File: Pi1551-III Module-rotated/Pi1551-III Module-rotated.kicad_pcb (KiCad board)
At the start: 2 copper layers, 100 x 100 mm, 35 parts, among them J1 DC IN, J3 TCBM, J4 Mini-DIN-7, J8 Module_Panel, M1 Mounting, M2 Mounting, M3 Mounting, M4 Mounting, Q1 MMBT3904, Q2 MMBT3904, Q3 MMBT3904, Q4 MMBT3904

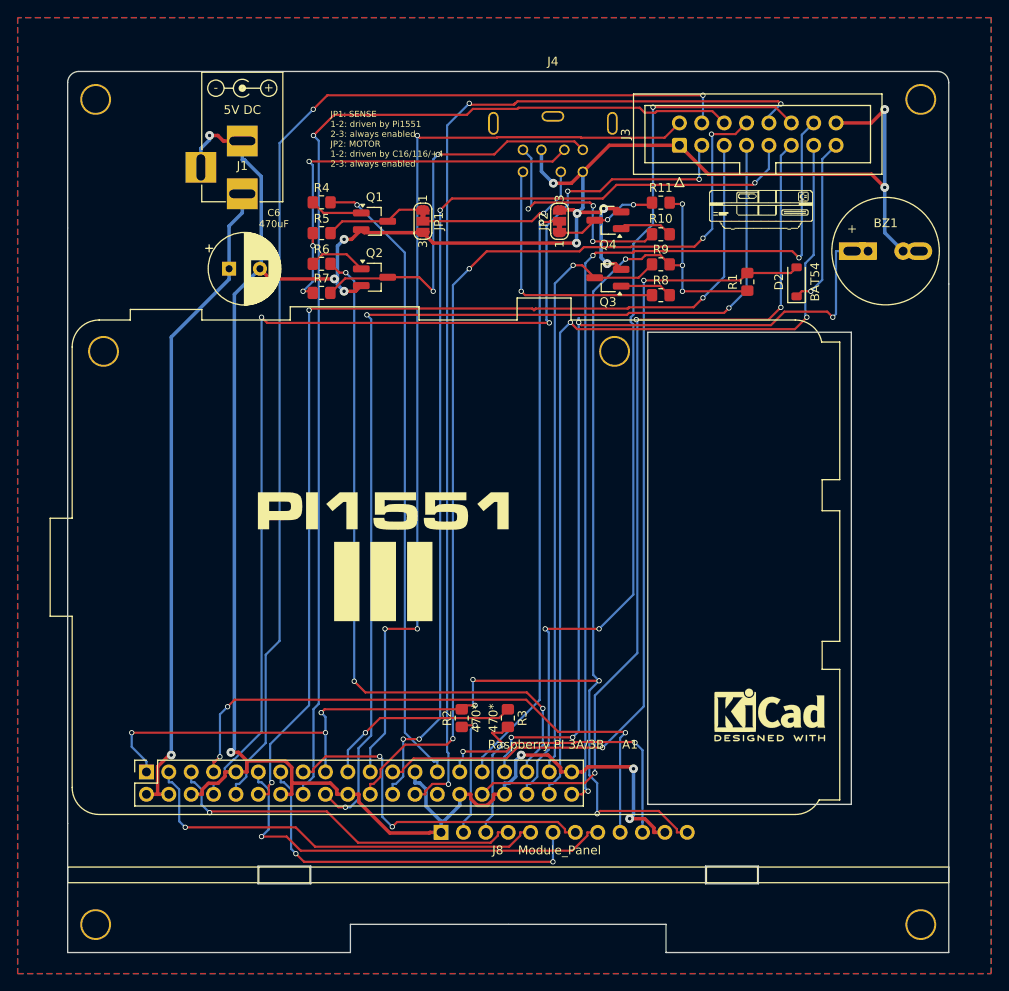
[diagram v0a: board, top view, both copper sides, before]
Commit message: all 10K resistors to 3.3K, JLPCB part numbers for 470R resistors, 1.2mm track width for 5V - as short as possible
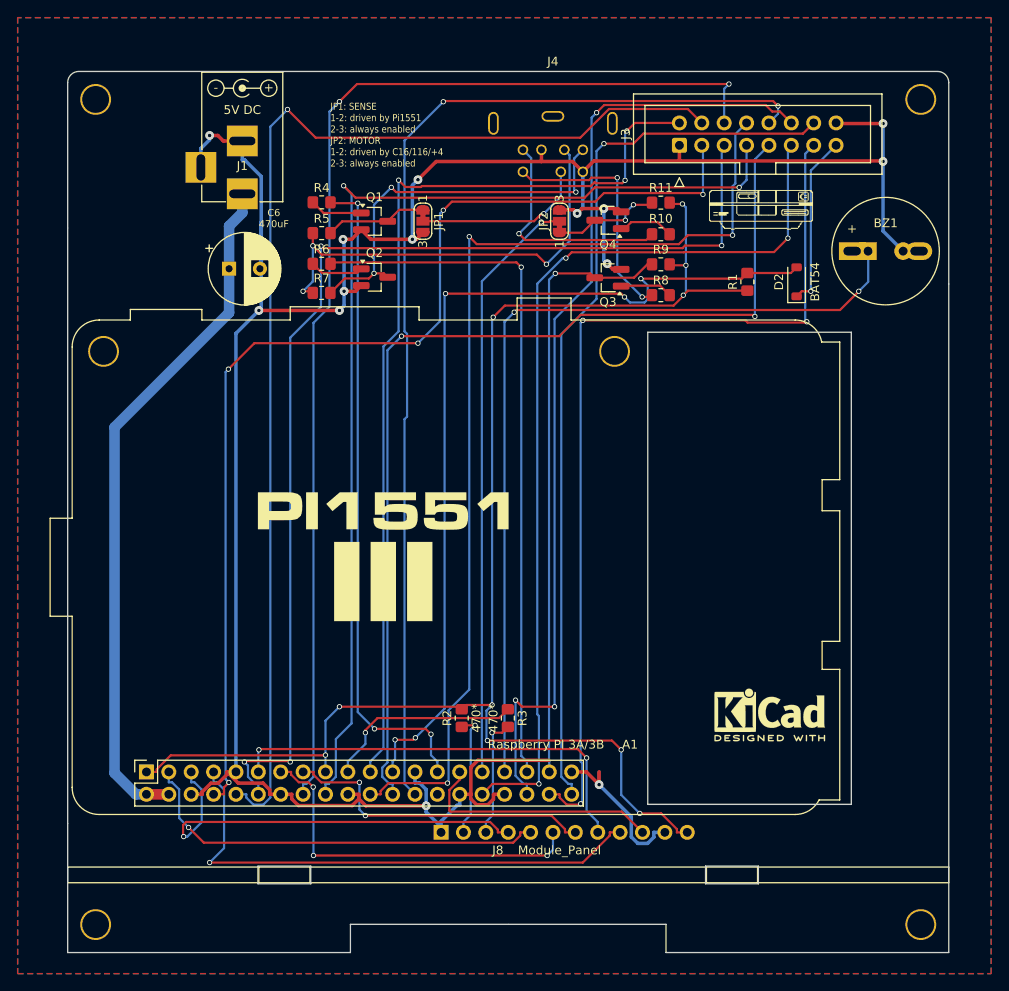
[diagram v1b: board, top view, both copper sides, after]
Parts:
- R1, R10, R11, R4, R5, R6, R7, R8, R9: value 10k -> 3.3K
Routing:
- net SW4_BACK: track 66.7 -> 59.9 mm, vias 3 -> 1
- net I2C_SCL: track 41.8 -> 48.2 mm
- net /DIO4: track 124.8 -> 130.2 mm, vias 1 -> 2
- net SW5_INSERT: track 33.0 -> 27.8 mm, vias 2 -> 0
- net /DIO3: track 122.4 -> 127.0 mm, vias 3 -> 4
- net /DIO6: track 112.0 -> 116.6 mm, vias 4 -> 3
- net /DIO2: track 129.7 -> 134.2 mm, vias 2 -> 1
- net /~{RESET_3V3}: track 98.1 -> 102.4 mm, vias 2 -> 5
- net /STATUS0: track 104.7 -> 108.9 mm
- net +5V: track 74.8 -> 78.9 mm, vias 1 -> 0
- net SW2_UP: track 39.9 -> 35.9 mm
- net /TAP_SENSE: track 71.5 -> 74.8 mm, vias 1 -> 3
- net /DIO7: track 111.7 -> 114.9 mm, vias 4 -> 2
- net /ACK: track 102.5 -> 105.5 mm, vias 2 -> 3
- net +3.3V: track 172.4 -> 169.8 mm, vias 11 -> 10
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
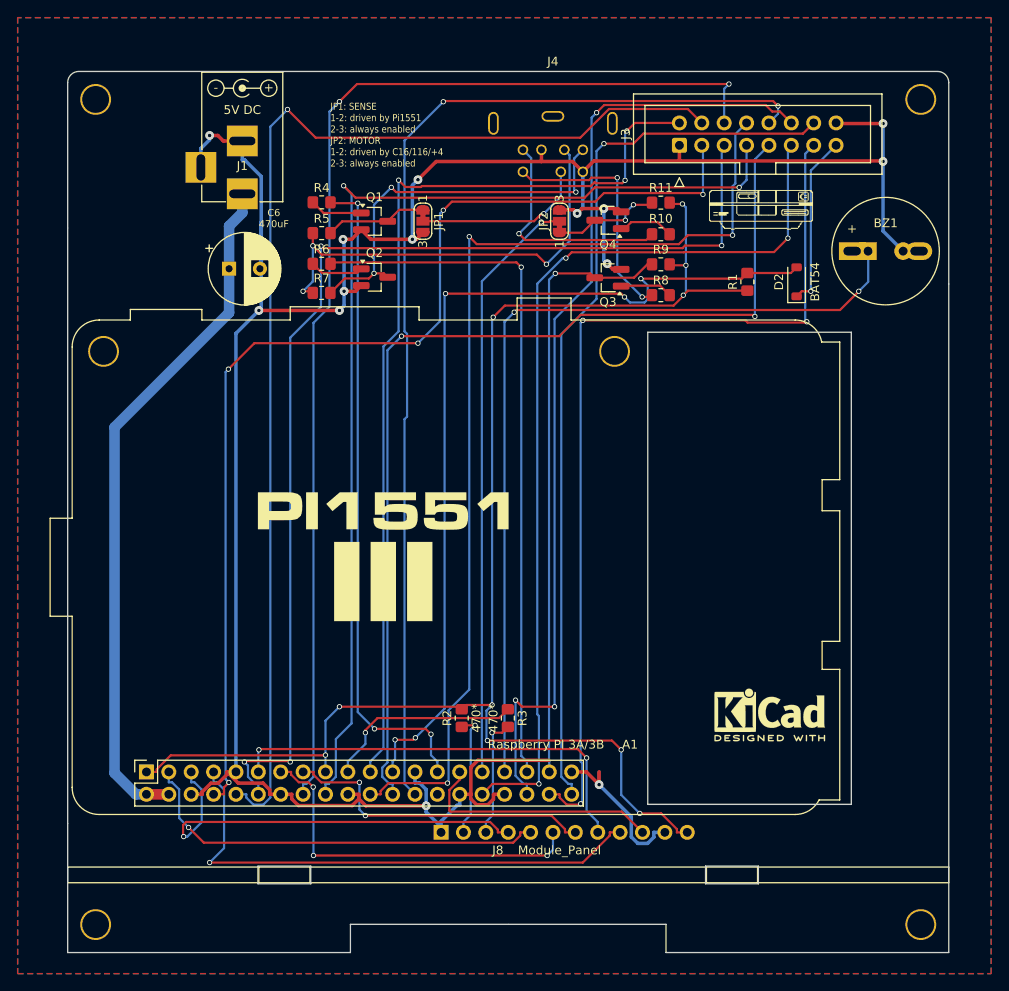
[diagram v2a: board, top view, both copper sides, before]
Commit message: revision 2 - pullups on all TCBM lines
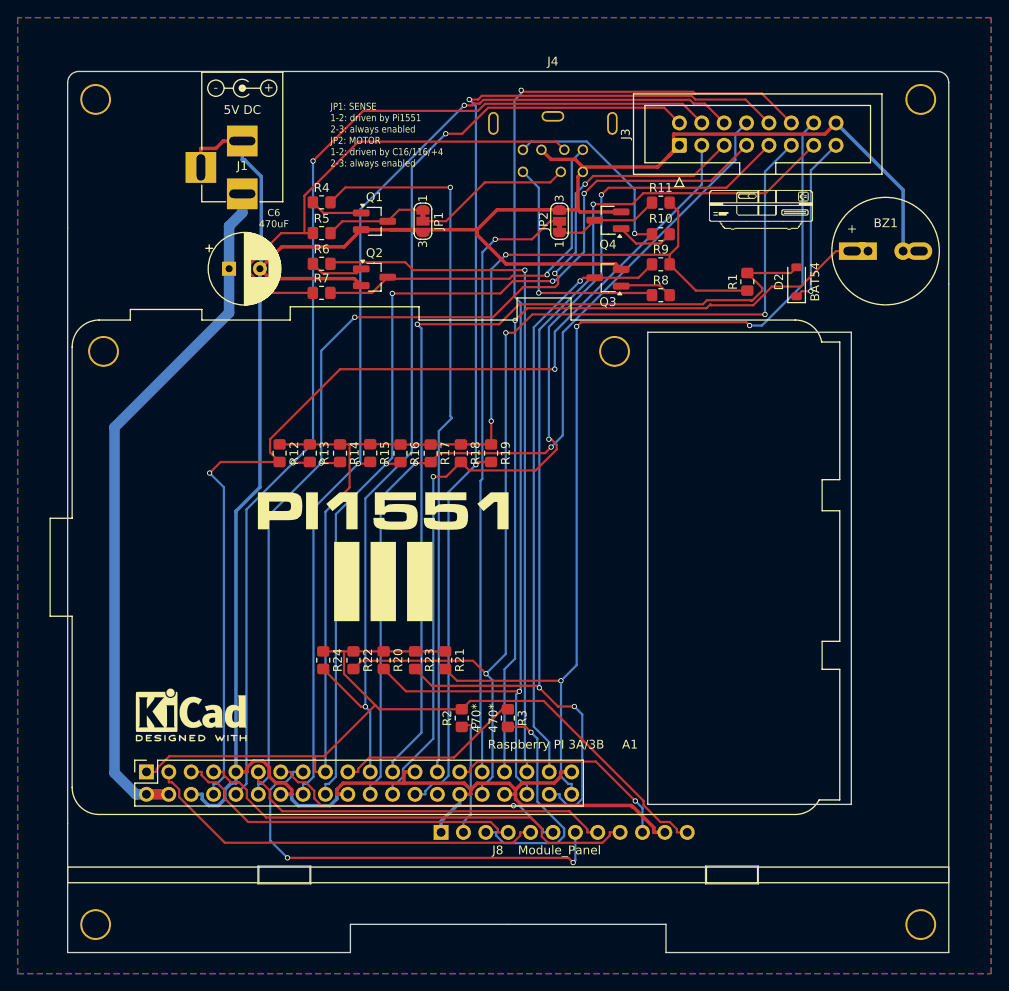
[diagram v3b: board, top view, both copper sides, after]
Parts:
- added R12: 3.3K, Resistor_SMD:R_0805_2012Metric_Pad1.20x1.40mm_HandSolder, F.Cu at (94.2, 97.9)
- added R13: 3.3K, Resistor_SMD:R_0805_2012Metric_Pad1.20x1.40mm_HandSolder, F.Cu at (97.7, 97.9)
- added R14: 3.3K, Resistor_SMD:R_0805_2012Metric_Pad1.20x1.40mm_HandSolder, F.Cu at (101.1, 97.9)
- added R15: 3.3K, Resistor_SMD:R_0805_2012Metric_Pad1.20x1.40mm_HandSolder, F.Cu at (104.5, 97.9)
- added R16: 3.3K, Resistor_SMD:R_0805_2012Metric_Pad1.20x1.40mm_HandSolder, F.Cu at (108.0, 97.9)
- added R17: 3.3K, Resistor_SMD:R_0805_2012Metric_Pad1.20x1.40mm_HandSolder, F.Cu at (111.4, 97.9)
- added R18: 3.3K, Resistor_SMD:R_0805_2012Metric_Pad1.20x1.40mm_HandSolder, F.Cu at (114.8, 97.9)
- added R19: 3.3K, Resistor_SMD:R_0805_2012Metric_Pad1.20x1.40mm_HandSolder, F.Cu at (118.2, 97.9)
- added R20: 3.3K, Resistor_SMD:R_0805_2012Metric_Pad1.20x1.40mm_HandSolder, F.Cu at (106.0, 121.4)
- added R21: 3.3K, Resistor_SMD:R_0805_2012Metric_Pad1.20x1.40mm_HandSolder, F.Cu at (113.0, 121.4)
- added R22: 3.3K, Resistor_SMD:R_0805_2012Metric_Pad1.20x1.40mm_HandSolder, F.Cu at (102.6, 121.4)
- added R23: 3.3K, Resistor_SMD:R_0805_2012Metric_Pad1.20x1.40mm_HandSolder, F.Cu at (109.6, 121.4)
- added R24: 3.3K, Resistor_SMD:R_0805_2012Metric_Pad1.20x1.40mm_HandSolder, F.Cu at (99.2, 121.4)
- moved REF2 65.7 mm to (84.2, 127.4)
- moved REF1 65.7 mm to (84.2, 127.6)
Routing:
- net +3.3V: track 169.8 -> 217.4 mm, vias 10 -> 3
- net /STATUS0: track 108.9 -> 130.2 mm, vias 3 -> 2
- net /DAV: track 105.1 -> 121.1 mm
- net /ACK: track 105.5 -> 120.7 mm
- net /DIO6: track 116.6 -> 102.1 mm, vias 3 -> 2
- net /STATUS1: track 101.3 -> 115.1 mm, vias 1 -> 3
- net SW2_UP: track 35.9 -> 49.5 mm
- net LED_ACT: track 13.8 -> 26.2 mm
- net /DIO4: track 130.2 -> 118.3 mm
- net /DIO3: track 127.0 -> 116.2 mm
- net /DIO2: track 134.2 -> 125.1 mm, vias 1 -> 2
- net /DIO5: track 121.9 -> 112.9 mm, vias 2 -> 4
- net SW4_BACK: track 59.9 -> 51.5 mm, vias 1 -> 0
- net I2C_SCL: track 48.2 -> 39.8 mm, vias 1 -> 0
- net /DIO1: track 124.9 -> 117.3 mm, vias 5 -> 2
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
